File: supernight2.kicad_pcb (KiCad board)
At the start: 4 copper layers, 87.2 x 56.2 mm, 74 parts, among them J2 Conn_02x04_Odd_Even, Q1 BC847C, Q2 DMN3010LK3, Q3 DMN3010LK3, SW1 SW_SPST, U1 ESP32, U2 LMR33640ADDA, U3 LMR33610ADDA, U4 EL7202CN

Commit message: ran most of the power
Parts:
- removed C3: 330uF, Capacitor_SMD:CP_Elec_10x10.5
- removed the REF** at (121.6, 99.7)
- added REF**: TerminalBlock_Phoenix_PT-1,5-6-5.0-H_1x06_P5.00mm_Horizontal, TerminalBlock_Phoenix:TerminalBlock_Phoenix_PT-1,5-6-5.0-H_1x06_P5.00mm_Horizontal, F.Cu at (120.2, 104.7)
- moved TH1 26.3 mm to (136.0, 89.3), turned to 270 degrees
- moved 12V_SW1 21.4 mm to (145.4, 92.1)
- moved R8 12.2 mm to (171.0, 72.1)
- moved C1 9.84 mm to (150.4, 78.9)
- moved 3V3_SW1 7.53 mm to (185.4, 107.3)
- moved Q2 5.41 mm to (133.0, 104.0), turned to 180 degrees
- moved REF** 3.83 mm to (129.4, 89.7)
- moved Q3 3.77 mm to (133.0, 95.3)
- moved C2 3.13 mm to (135.8, 78.9)
- moved C22 2.07 mm to (157.4, 108.7)
- moved L1 2.02 mm to (159.4, 101.0)
- moved C20 2.00 mm to (163.4, 108.7)
- moved C21 2.00 mm to (167.0, 101.2)
- moved REF** 1.57 mm to (129.4, 109.5), turned to 270 degrees
- moved C19 0.87 mm to (174.4, 100.3)
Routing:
- net +3V3: track 0.00 -> 25.1 mm, vias 0 -> 13
- net +12V: track 0.00 -> 24.9 mm, vias 6 -> 8
- net ESP_SLP_L: track 0.00 -> 24.9 mm, vias 0 -> 2
- net 12v_EN: track 0.00 -> 23.7 mm, vias 0 -> 2
- net /Power Supply/12V_CBOOT: track 0.00 -> 5.03 mm
- net /Power Supply/3V3_CBOOT: track 0.00 -> 4.68 mm
- net OLED_SCL: track 0.00 -> 3.36 mm, vias 0 -> 1
- net OLED_SDA: track 0.00 -> 3.12 mm, vias 0 -> 1
- net /Power Supply/12V_5V_LDO: track 0.00 -> 2.77 mm
- net /MOSFET_DRIVE/CH1_FET_DRV_R: track 3.24 -> 5.95 mm
- net /Power Supply/3v3_5V_LDO: track 0.00 -> 2.27 mm
- net /MOSFET_DRIVE/CH2_FET_DRV_R: track 4.48 -> 6.73 mm
- net VDD: track 0.00 -> 2.20 mm, vias 0 -> 13
- net /VDD_SENSE_R: track 0.00 -> 1.82 mm
- added copper zone on F.Cu, net +3V3
- added copper zone on In2.Cu, net +3V3
- added copper zone on F.Cu, net /Power Supply/12V_FB
- added copper zone on F.Cu, net /Power Supply/12V_SW
- added copper zone on F.Cu, net /Power Supply/3V3_FB
- added copper zone on F.Cu, net /Power Supply/3V3_SW
- added copper zone on In2.Cu, net VDD

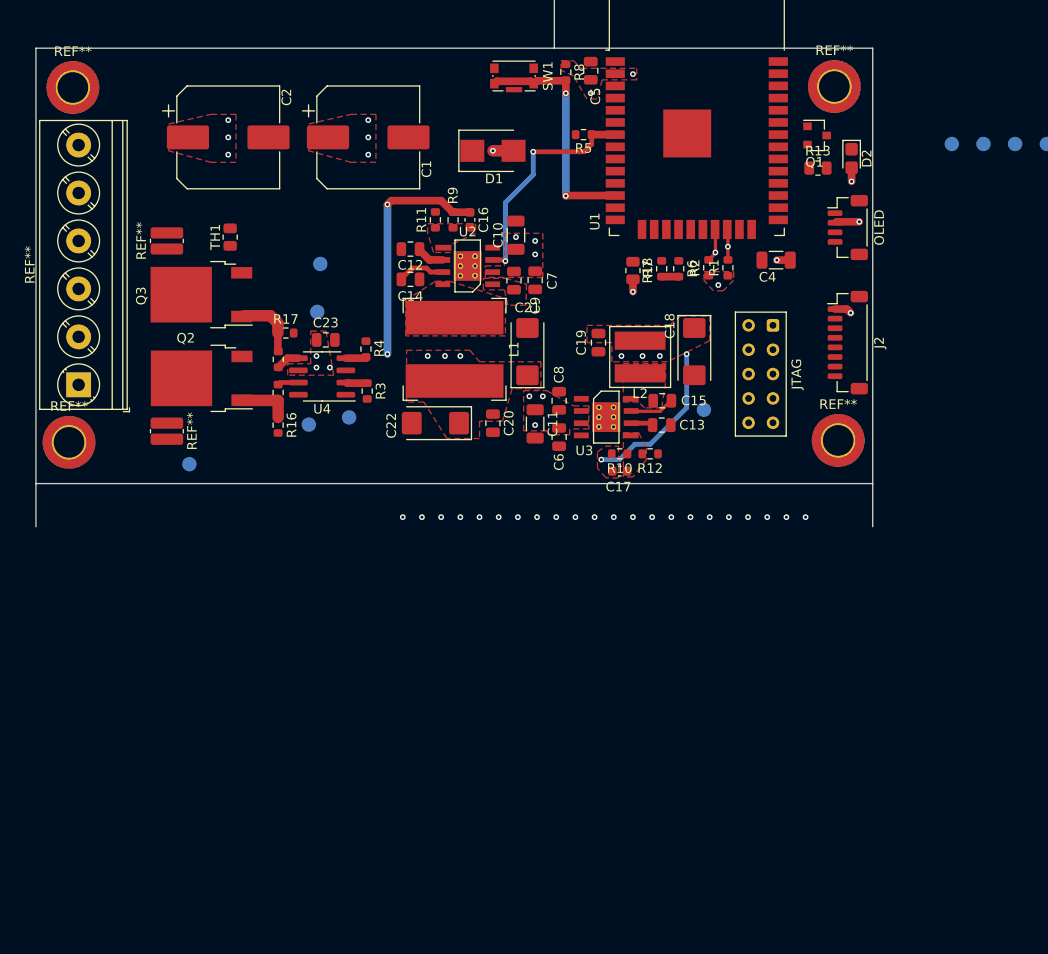
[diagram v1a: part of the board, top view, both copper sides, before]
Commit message: corrected esp32 pins and buck layout
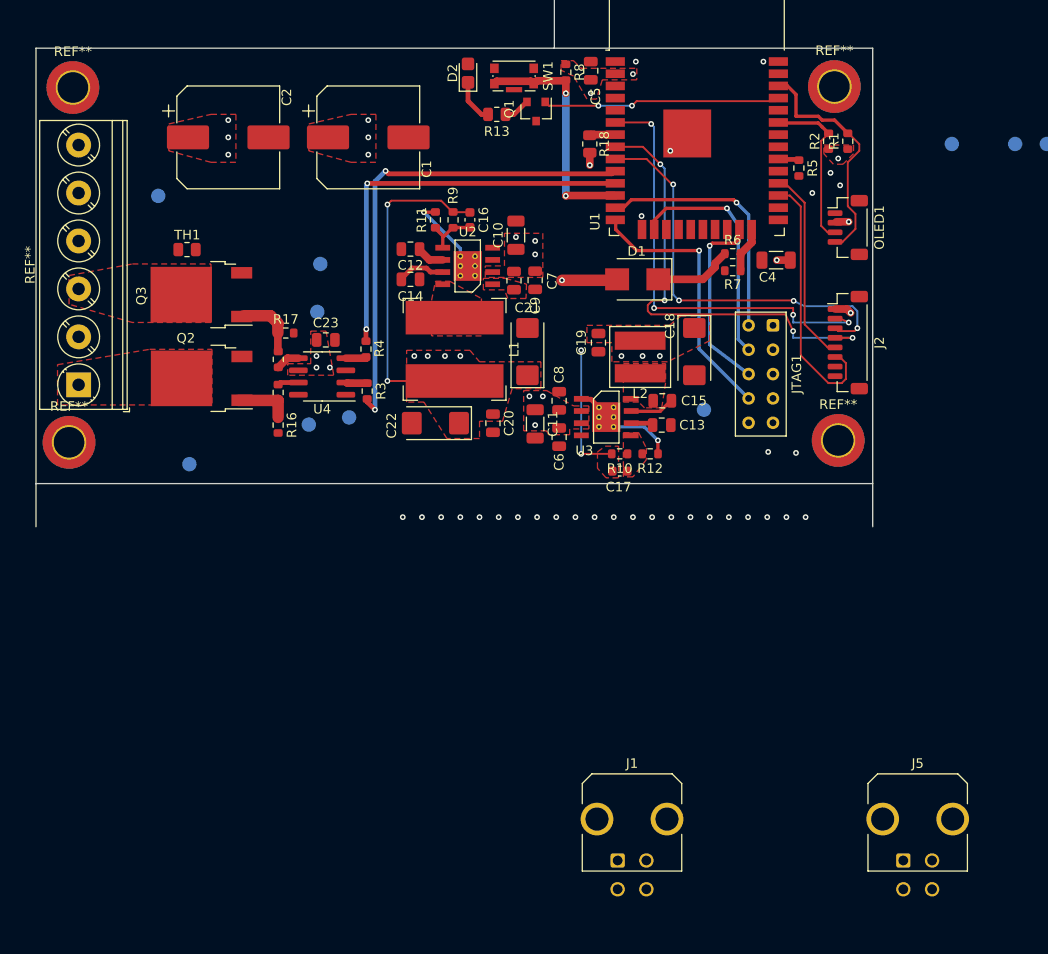
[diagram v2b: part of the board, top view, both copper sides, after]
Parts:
- removed the REF** at (129.4, 89.7)
- removed the REF** at (129.4, 109.5)
- added J1: 43045-0421, Connector_Molex:Molex_Micro-Fit_3.0_43045-0421_2x02-1MP_P3.00mm_Horizontal, F.Cu at (176.4, 154.3)
- added J5: 43045-0421, Connector_Molex:Molex_Micro-Fit_3.0_43045-0421_2x02-1MP_P3.00mm_Horizontal, F.Cu at (206.2, 154.3)
- moved TP1 86.2 mm to (128.5, 85.0)
- moved D2 41.0 mm to (160.8, 72.2), turned to 90 degrees
- moved R13 34.0 mm to (163.8, 76.5), turned to 0 degrees
- moved Q1 29.4 mm to (167.9, 76.2), turned to 270 degrees
- moved R5 22.7 mm to (195.3, 82.1), turned to 270 degrees
- moved D1 20.2 mm to (178.5, 93.7), turned to 180 degrees
- moved R1 18.2 mm to (200.4, 79.3)
- moved R2 18.2 mm to (198.4, 79.3)
- moved R18 13.9 mm to (173.5, 79.6)
- moved R7 7.41 mm to (188.4, 92.8), turned to 180 degrees
- moved R6 5.84 mm to (188.4, 91.0), turned to 0 degrees
- moved TH1 4.68 mm to (131.5, 90.6), turned to 180 degrees
- renumbered JTAG to JTAG1, OLED to OLED1
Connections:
- 3V3_PWGD1 pad 1: ESP_EN -> 3V3_PWGD
- R1 pad 2: OLED_SDA -> OLED_SCL
- R2 pad 2: OLED_SCL -> OLED_SDA
- U1 pad 21: OLED_SCL -> Net-(U1-Pad21)
- U1 pad 22: OLED_SDA -> Net-(U1-Pad22)
- U1 pad 27: Net-(U1-Pad27) -> ROT2_B
- U1 pad 28: Net-(U1-Pad28) -> ROT2_A
- U1 pad 3: ESP_EN -> 3V3_PWGD
- U1 pad 30: TEMP_FB -> 12v_EN
- U1 pad 33: ROT2_B -> OLED_SDA
- U1 pad 36: ROT2_A -> OLED_SCL
- U1 pad 7: 12v_EN -> TEMP_FB
- U3 pad 4: ESP_EN -> 3V3_PWGD
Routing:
- net /CH1_SIG: track 0.00 -> 51.0 mm, vias 0 -> 2
- net ROT1_B: track 0.00 -> 47.5 mm, vias 0 -> 4
- net BTN_SEL_1: track 0.00 -> 46.3 mm, vias 0 -> 4
- net ROT1_A: track 0.00 -> 42.8 mm, vias 0 -> 4
- net /CH2_SIG: track 0.00 -> 42.4 mm, vias 0 -> 2
- net TDI: track 0.00 -> 28.1 mm, vias 0 -> 1
- net ROT2_B: track 0.00 -> 27.4 mm
- net TMS: track 0.00 -> 26.7 mm, vias 0 -> 1
- net ESP_TX: track 0.00 -> 24.8 mm, vias 0 -> 2
- net TCK: track 0.00 -> 24.6 mm, vias 0 -> 1
- net 12v_EN: track 23.7 -> 2.33 mm, vias 2 -> 0
- net OLED_SCL: track 3.36 -> 24.7 mm, vias 1 -> 0
- net ROT2_A: track 0.00 -> 20.3 mm
- net TDO: track 0.00 -> 19.6 mm, vias 0 -> 1
- net GND: track 0.00 -> 16.1 mm, vias 22 -> 33
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- added copper zone on F.Cu, net /MOSFET_DRIVE/LED_L_1
- added copper zone on F.Cu, net /MOSFET_DRIVE/LED_L_2
- removed copper zone on F.Cu, net /Power Supply/12V_FB

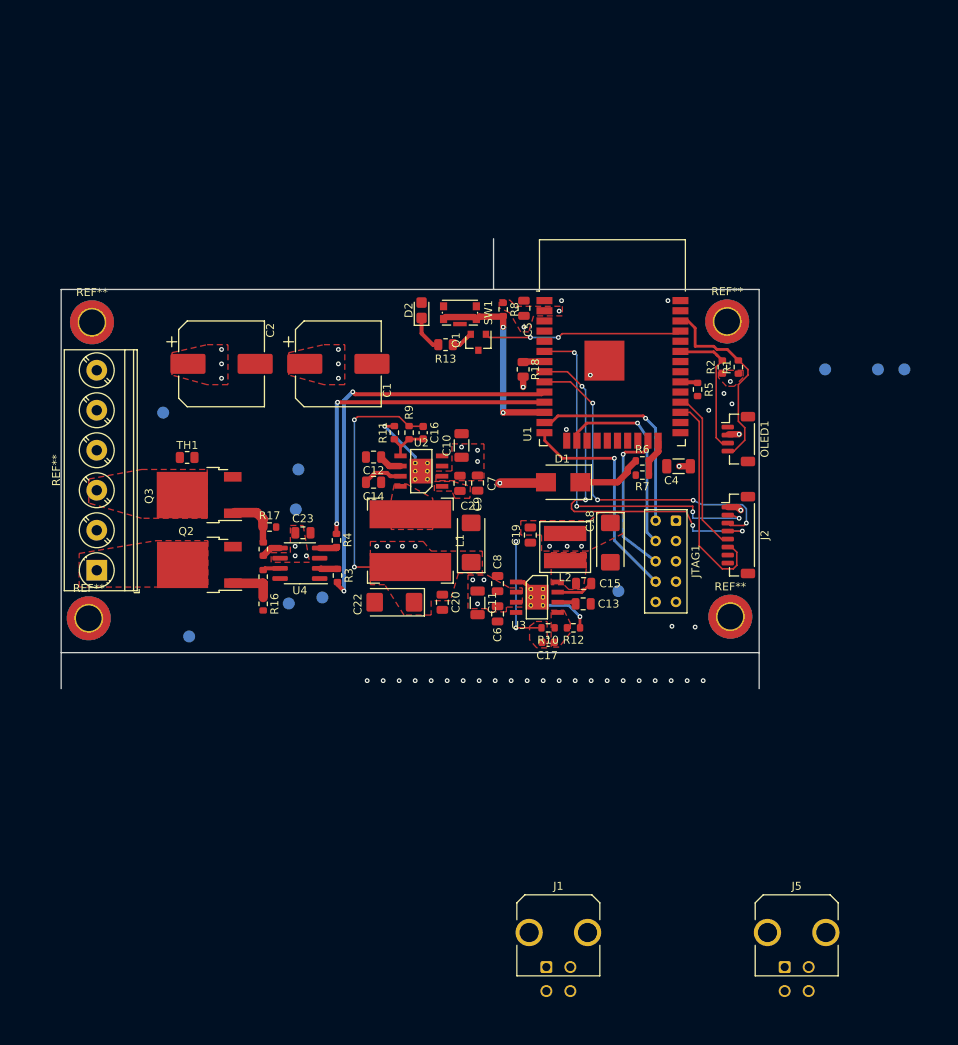
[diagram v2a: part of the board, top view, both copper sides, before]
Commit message: re-linked refs from brd to sch
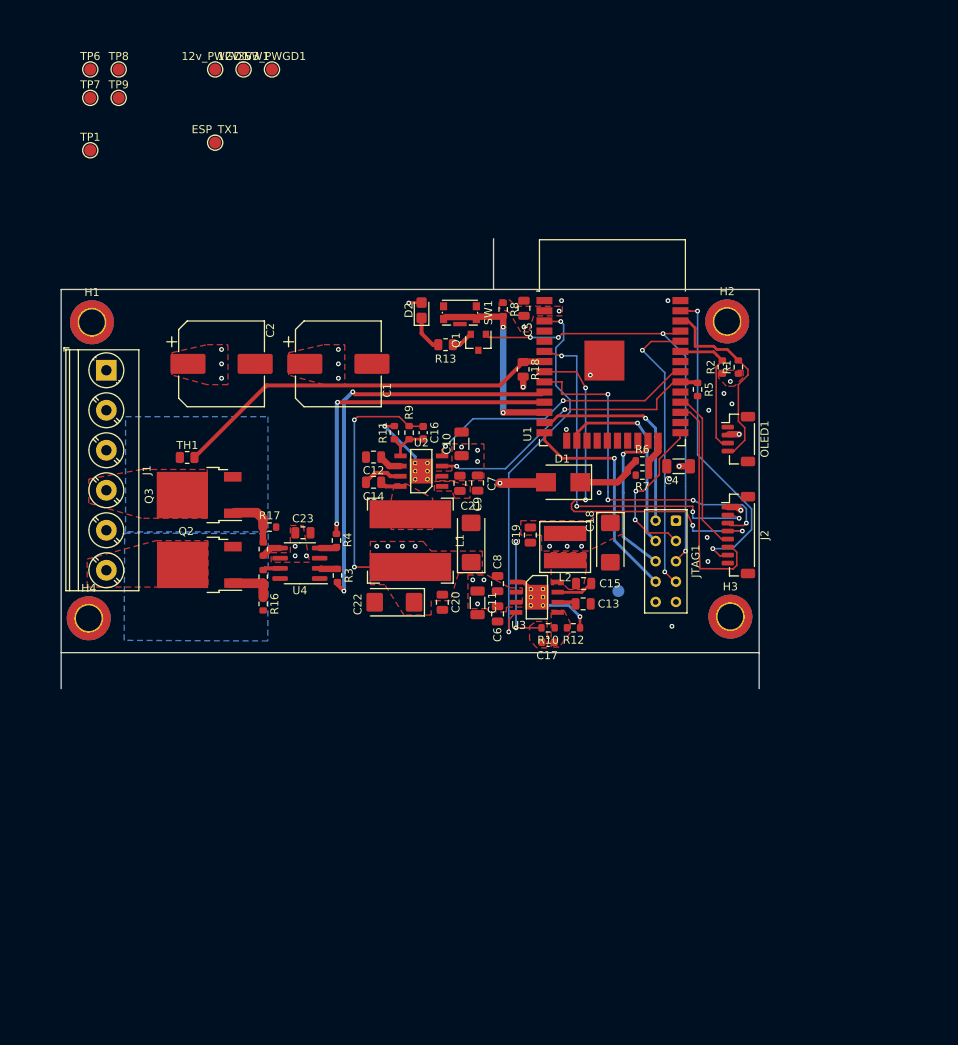
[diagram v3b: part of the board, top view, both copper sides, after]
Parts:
- removed the J1 at (176.4, 154.3)
- removed J5: 43045-0421, Connector_Molex:Molex_Micro-Fit_3.0_43045-0421_2x02-1MP_P3.00mm_Horizontal
- removed REF** (x2): MountingHole_3.2mm_M3_ISO14580_Pad_TopBottom, MountingHole:MountingHole_3.2mm_M3_ISO14580_Pad_TopBottom
- added H2: MountingHole_Pad, MountingHole:MountingHole_3.2mm_M3_ISO14580_Pad_TopBottom, F.Cu at (199.0, 73.6)
- added H3: MountingHole_Pad, MountingHole:MountingHole_3.2mm_M3_ISO14580_Pad_TopBottom, F.Cu at (199.4, 110.5)
- 12V_SW1, 12v_PWGD1, 3V3_PWGD1, ESP_TX1, TP1, TP6, TP7, TP8, TP9: moved to F.Cu
- H1, H4: renamed from REF**; value MountingHole_3.2mm_M3_ISO14580_Pad_TopBottom -> MountingHole_Pad
- J1: renamed from REF**; value TerminalBlock_Phoenix_PT-1,5-6-5.0-H_1x06_P5.00mm_Horizontal -> Conn_01x06_Female
- moved 12v_PWGD1 94.0 mm to (135.0, 42.1)
- moved 3V3_PWGD1 84.5 mm to (142.1, 42.1)
- moved ESP_TX1 81.3 mm to (135.0, 51.2)
- moved TP8 71.4 mm to (122.9, 42.1), turned to 0 degrees
- moved TP7 67.9 mm to (119.4, 45.6), turned to 0 degrees
- moved TP9 67.4 mm to (122.9, 45.6), turned to 0 degrees
- moved TP6 60.7 mm to (119.4, 42.1), turned to 0 degrees
- moved 12V_SW1 50.5 mm to (138.6, 42.1), turned to 0 degrees
- moved TP1 34.0 mm to (119.4, 52.2), turned to 0 degrees
- moved J1 25.0 mm to (121.4, 79.7), turned to 270 degrees
- moved C10 0.20 mm to (165.8, 88.9)
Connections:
- H1 pad 1: (no net) -> GND
- H4 pad 1: (no net) -> GND
- J1 pad 1: /MOSFET_DRIVE/LED_L_1 -> VDD
- J1 pad 2: VDD -> GND
- J1 pad 3: /MOSFET_DRIVE/LED_L_2 -> VDD
- J1 pad 4: VDD -> /MOSFET_DRIVE/LED_L_2
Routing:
- net 3V3_PWGD: track 0.00 -> 48.1 mm, vias 0 -> 2
- net TEMP_FB: track 2.69 -> 48.9 mm
- net BTN_SEL_2: track 0.00 -> 40.4 mm, vias 0 -> 2
- net ESP_RX: track 0.00 -> 36.1 mm, vias 0 -> 2
- net 12v_EN: track 2.33 -> 37.4 mm, vias 0 -> 2
- net 12v_PWGD: track 0.00 -> 34.6 mm, vias 0 -> 2
- net ESP_TX: track 24.8 -> 55.0 mm, vias 2 -> 4
- net ESP_BOOT_L: track 0.00 -> 19.9 mm, vias 0 -> 2
- net +3V3: track 19.8 -> 34.7 mm, vias 12 -> 13
- net /Power Supply/12V_SW: track 0.00 -> 2.58 mm
- net ROT1_A: track 42.8 -> 44.7 mm
- net ROT2_B: track 27.4 -> 29.0 mm
- net GND: vias 33 -> 14
- added copper zone on B.Cu, net /MOSFET_DRIVE/LED_L_1
- added copper zone on B.Cu, net /MOSFET_DRIVE/LED_L_2
